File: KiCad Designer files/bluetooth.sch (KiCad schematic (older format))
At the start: 26 parts, among them U1 O, U10 O, U11 O, U12 O, U13 O, U14 O, U15 O, U16 O, U17 O, U18 O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

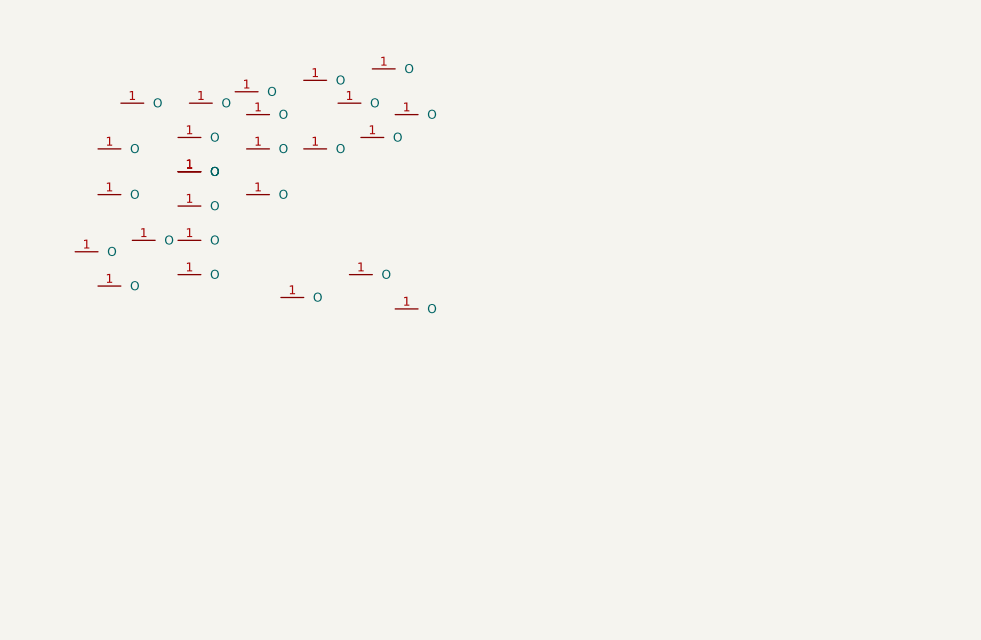
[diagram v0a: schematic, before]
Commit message: added antenna to main pcb
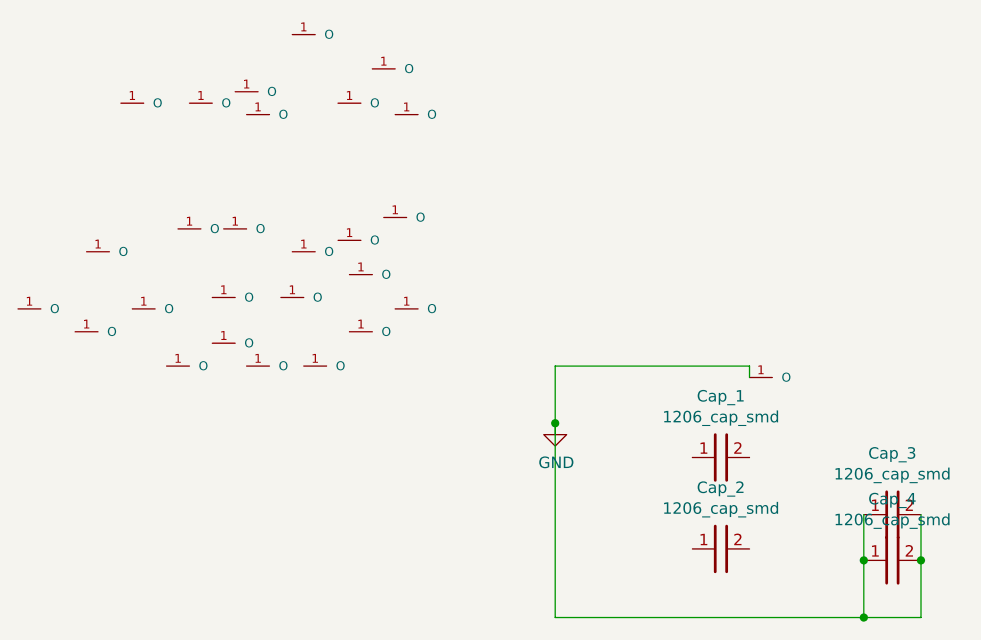
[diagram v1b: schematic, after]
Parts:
- added Cap_1, Cap_2, Cap_3, Cap_4: 1206_cap_smd, Capacitors_smd:1206_cap_smd, symbol Capacitors_smd:1206_cap_smd
- added U8: O, ICs:Ο, symbol ICs:O
- renumbered U22 to U102
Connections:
- net at U2.1 (O): no longer U15.1 (O)
- new net GND: Cap_3.1, Cap_3.2, Cap_4.1, Cap_4.2, U8.1 (O)
